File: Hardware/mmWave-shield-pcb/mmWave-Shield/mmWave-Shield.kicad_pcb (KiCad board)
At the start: 4 copper layers, 21 x 15 mm, 34 parts, among them J3 DF40HC_3.0_-40DS-0.4V_51, J4 DF40HC_3.0_-50DS-0.4V_51, U1 TPS22916CYFPR, U2 TPS22916CYFPR, X1 KC2016K80.0000C1GE00

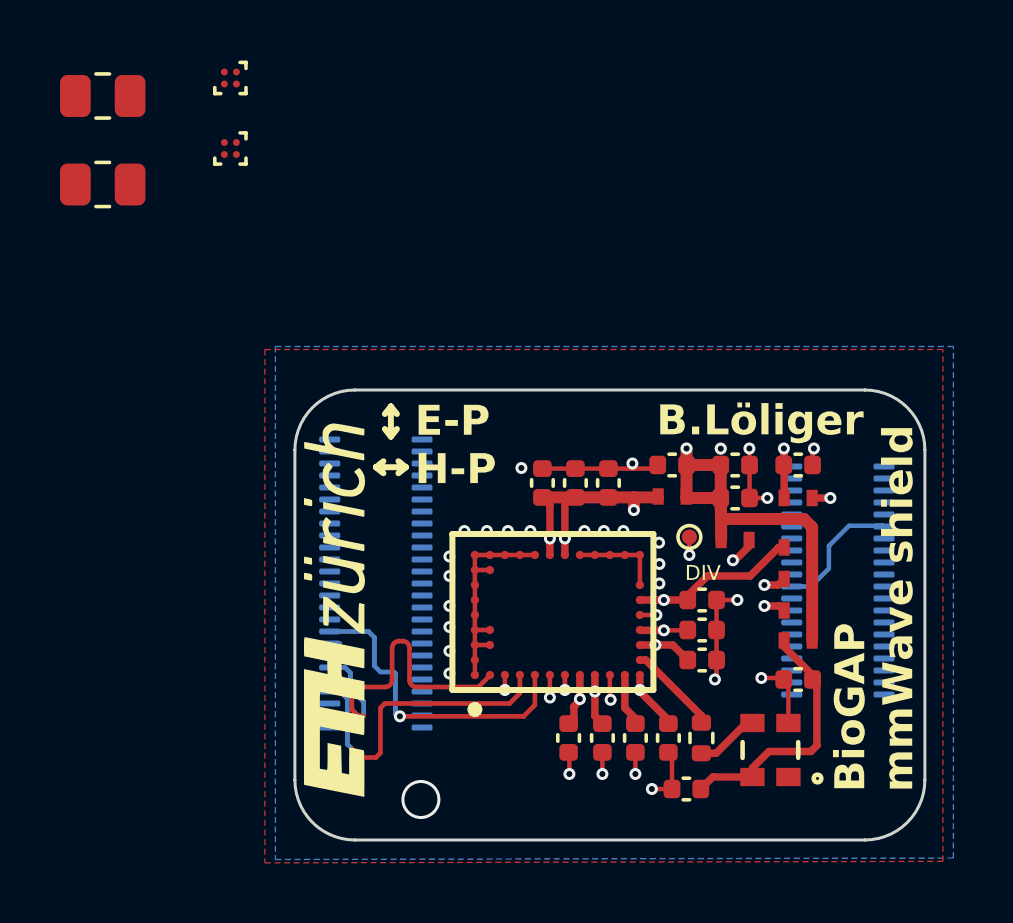
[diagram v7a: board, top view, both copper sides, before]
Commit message: finished adding power controll
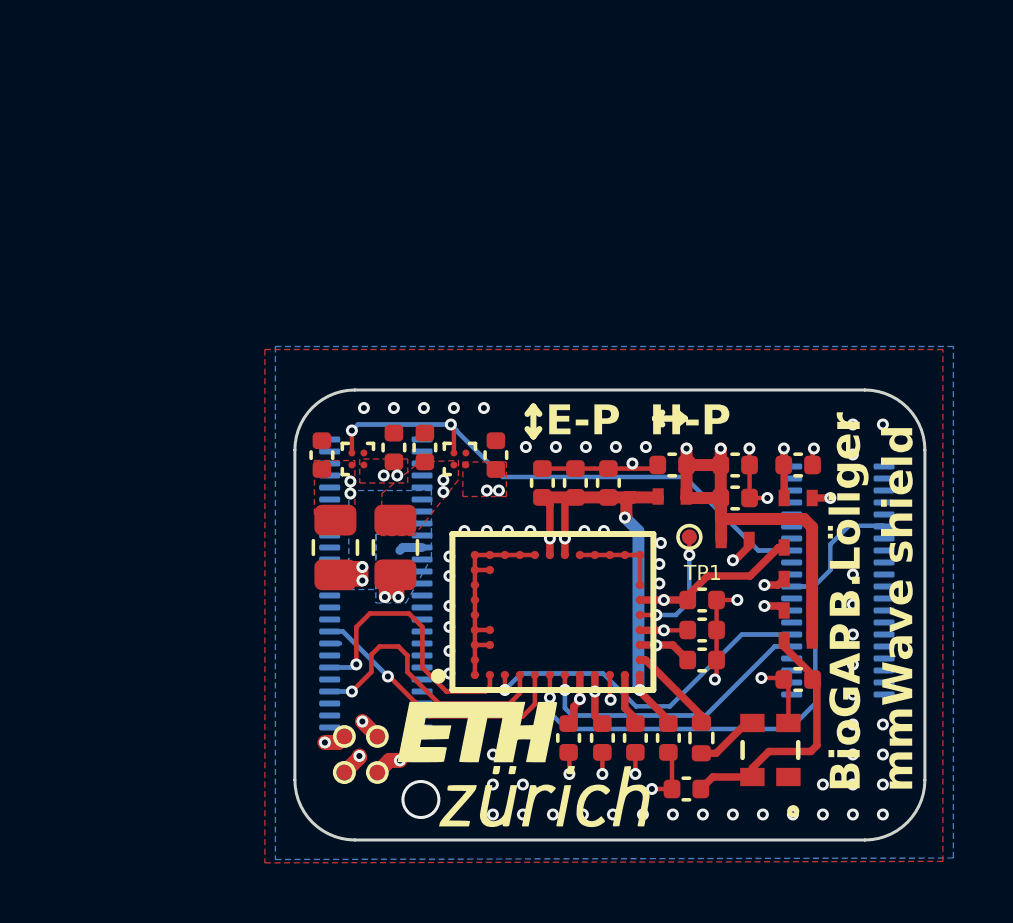
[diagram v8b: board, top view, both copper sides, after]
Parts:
- added C17: 47uF, Capacitor_SMD:C_0402_1005Metric, F.Cu at (140.2, 95.6)
- added C18: 1uF, Capacitor_SMD:C_0402_1005Metric, F.Cu at (137.8, 95.8)
- added C19: 47uF, Capacitor_SMD:C_0402_1005Metric, F.Cu at (143.6, 95.8)
- added C20: 1uF, Capacitor_SMD:C_0402_1005Metric, F.Cu at (141.2, 95.6)
- added TP2: TestPoint, TestPoint:TestPoint_Pad_D1.0mm, F.Cu at (138.6, 106.4)
- added TP3: TestPoint, TestPoint:TestPoint_Pad_D1.0mm, F.Cu at (139.7, 106.4)
- added TP4: TestPoint, TestPoint:TestPoint_Pad_D1.0mm, F.Cu at (139.7, 105.2)
- added TP5: TestPoint, TestPoint:TestPoint_Pad_D1.0mm, F.Cu at (138.6, 105.2)
- moved R3 16.9 mm to (138.2, 98.9), turned to -90 degrees
- moved R4 15.5 mm to (140.2, 98.9), turned to -90 degrees
- moved U1 13.4 mm to (139.0, 96.0), turned to 180 degrees
- moved U2 12.9 mm to (142.4, 96.0), turned to 180 degrees
- moved REF** 6.73 mm to (143.4, 105.3), turned to 0 degrees
- renumbered DIV to TP1
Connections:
- net Net-(U1-VIN) renamed /sensor/sw_in_1v8
- net Net-(U2-VIN) renamed /sensor/sw_in_3v3
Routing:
- net VDD_A: track 2.54 -> 21.6 mm
- net nRF_P0.07/AMUX: track 0.00 -> 18.2 mm, vias 0 -> 2
- net GAP_GPIO46: track 5.12 -> 19.0 mm
- net nRF_P0.12_GAP_GPIO64: track 0.50 -> 11.7 mm
- net /sensor/sw_in_3v3: track 0.00 -> 11.0 mm, vias 0 -> 3
- net VDD_LF: track 2.41 -> 13.3 mm
- net VD2: track 0.00 -> 10.8 mm, vias 0 -> 3
- net /sensor/sw_in_1v8: track 0.00 -> 10.2 mm, vias 0 -> 3
- net 1V8_Connector: track 0.00 -> 9.43 mm, vias 0 -> 3
- net nRF_P1.11_GAP_GPIO63: track 0.50 -> 9.72 mm
- net VDD_D: track 2.50 -> 10.6 mm
- net VDD_RF: track 10.6 -> 17.1 mm
- net VDD_PLL: track 2.55 -> 5.80 mm
- net /sensor/DIV_OUT: track 1.15 -> 3.99 mm, vias 4 -> 2
- net SPI_A_CLK: track 10.9 -> 9.16 mm, vias 0 -> 1
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- added copper zone on F.Cu, net /sensor/sw_in_1v8
- added copper zone on F.Cu, net /sensor/sw_in_3v3
- added copper zone on F.Cu, net 1V8
- added copper zone on B.Cu, net 1V8_Connector
- added copper zone on F.Cu, net 3V3
- added copper zone on In2.Cu, net 3V3
- added copper zone on B.Cu, net VD2
- removed copper zone on In2.Cu, net VD2
